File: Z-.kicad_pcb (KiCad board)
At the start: 4 copper layers, 98 x 98 mm, 147 parts, among them J1 200528-0100, J2 U.FL, J3 U.FL, J5 Conn_01x02, K1 IM02, Q1 NX3008NBKS, Q10 MBT2222ADW1T1, Q11 NX3008NBKS, Q12 MBT2222ADW1T1, Q13 IRLML2803, Q15 IRFTS9342PBF, Q17 IRFTS9342PBF, Q19 IRFTS9342PBF, Q2 MBT2222ADW1T1, Q20 IRLML2803, Q21 SiRA99DP, Q3 NX3008NBKS, Q4 MBT2222ADW1T1, Q5 NX3008NBKS, Q6 MBT2222ADW1T1, Q7 NX3008NBKS, Q8 MBT2222ADW1T1, Q9 NX3008NBKS, U1 OPT4003DNPRQ1, U2 PCA9633DP2, U3 USBLC6-2P6, U4 DRV8235RTER

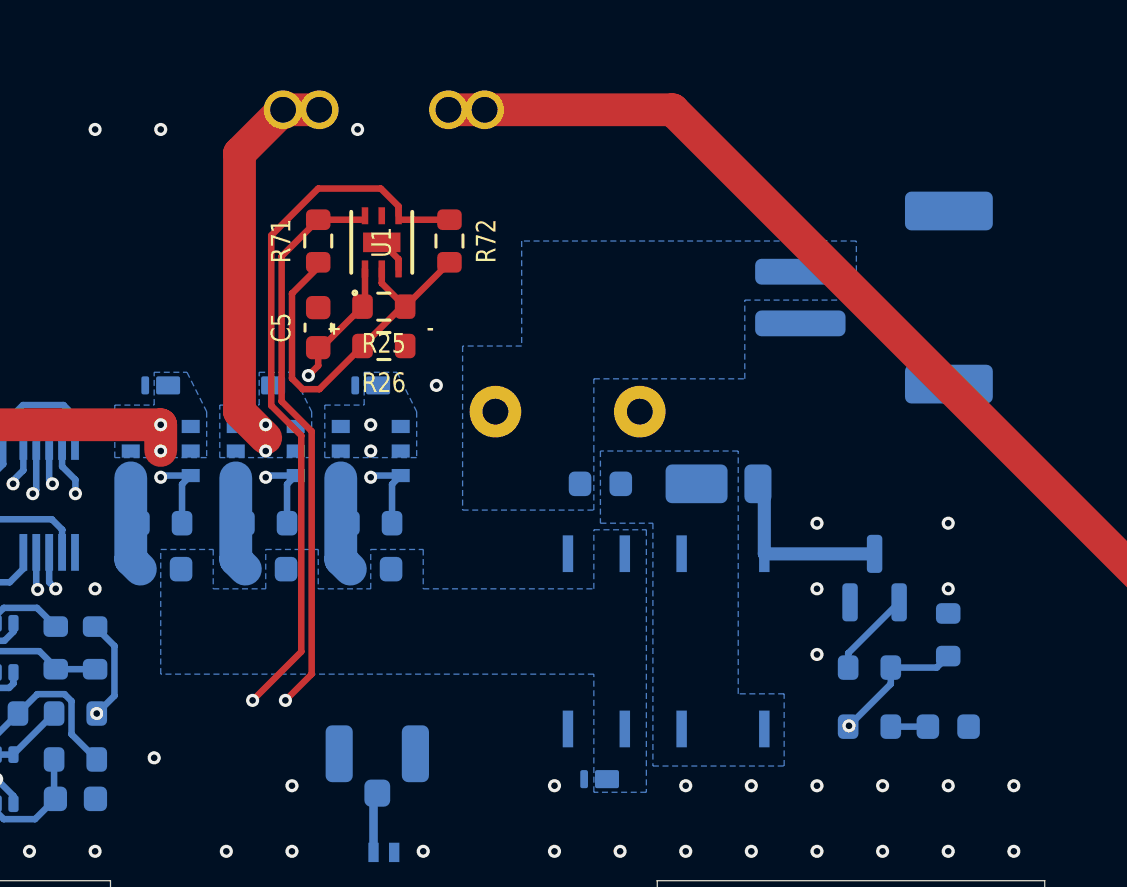
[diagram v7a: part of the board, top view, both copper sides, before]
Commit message: Updated burnwire circuitry and layout
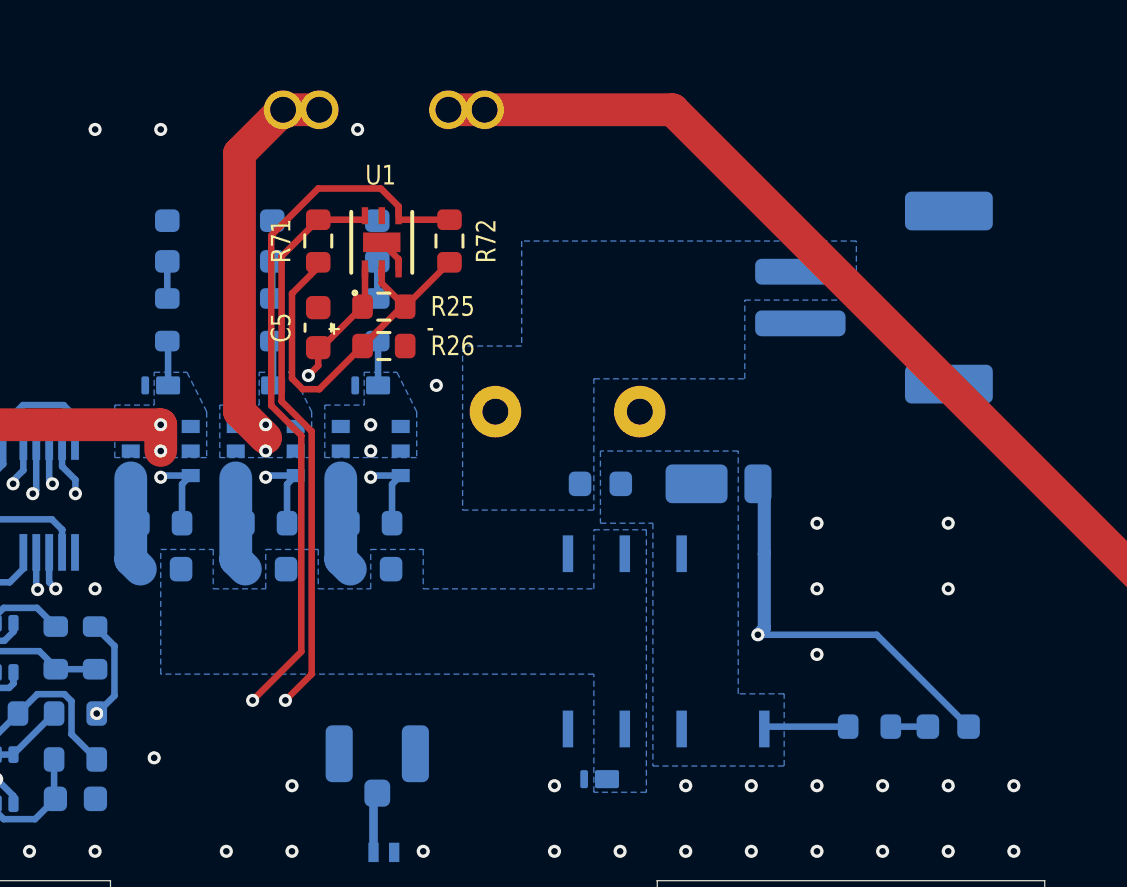
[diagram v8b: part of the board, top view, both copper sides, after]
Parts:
- removed Q13: IRLML2803, Package_TO_SOT_SMD:SOT-23
- added D10: GREEN, LED_SMD:LED_0603_1608Metric, B.Cu at (148.1, 63.5)
- added D11: GREEN, LED_SMD:LED_0603_1608Metric, B.Cu at (152.1, 63.5)
- added D9: GREEN, LED_SMD:LED_0603_1608Metric, B.Cu at (144.0, 63.5)
- added R73: 2.7k, Resistor_SMD:R_0603_1608Metric, B.Cu at (152.1, 66.5)
- R69: value 10k -> 2.7k
- R70: value 4k7 -> 2.7k
- moved R69 32.6 mm to (144.0, 66.5), turned to 90 degrees
- moved R70 26.7 mm to (148.1, 66.5), turned to 90 degrees
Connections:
- D1 pad 1: GND -> BURN_RELAY_A
- D7 pad 2: Net-(D7-A) -> BURN_RELAY_A
- K1 pad 8: Net-(D7-A) -> BURN_RELAY_A
- R68 pad 1: BURN_RELAY_A -> Net-(D7-K)
- R69 pad 1: GND -> /Burn Wires/VBURN1
- R69 pad 2: BURN_RELAY_A -> Net-(D9-A)
- R70 pad 1: BURN_RELAY_A -> /Burn Wires/VBURN2
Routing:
- net Net-(D7-A): track 7.08 -> 0.00 mm
- net BURN_RELAY_A: track 41.3 -> 46.8 mm
- net Net-(D7-K): track 0.00 -> 3.33 mm
- net Net-(D10-A): track 3.34 -> 1.44 mm
- net /Burn Wires/VBURN3: track 26.3 -> 28.0 mm
- net /Burn Wires/VBURN2: track 16.2 -> 18.0 mm
- net /Burn Wires/VBURN1: track 43.0 -> 44.8 mm
- net Net-(D11-A): track 0.00 -> 1.54 mm
- net Net-(D9-A): track 0.00 -> 1.44 mm
